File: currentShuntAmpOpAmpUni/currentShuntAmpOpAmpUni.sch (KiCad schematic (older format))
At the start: 10 parts, among them Q1 2N3906, U1 AD822A

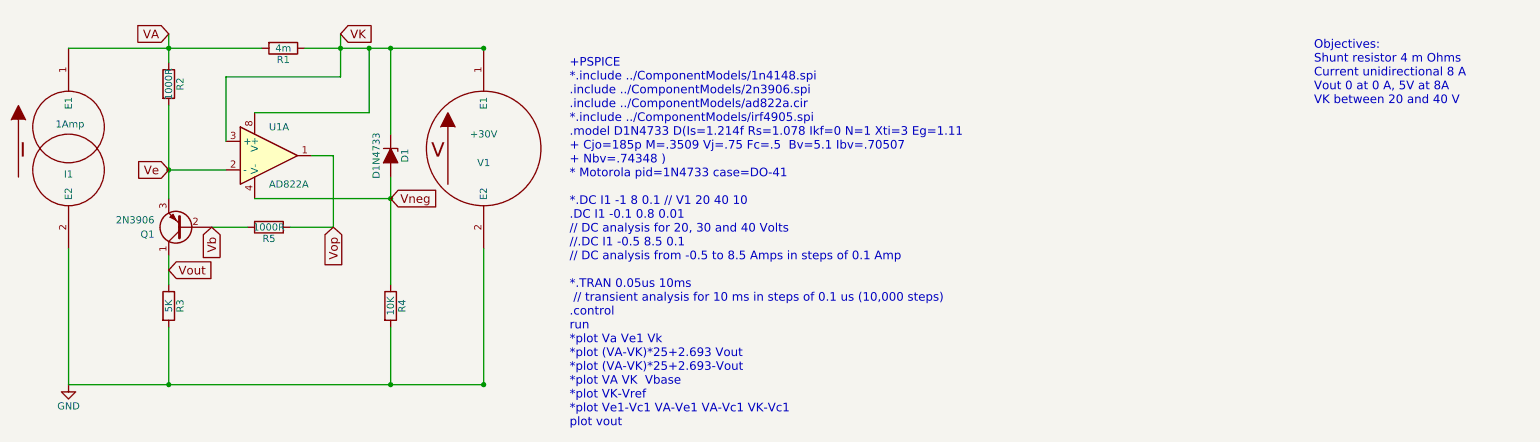
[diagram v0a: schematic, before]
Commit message: completed first current shunt amp using an op amp
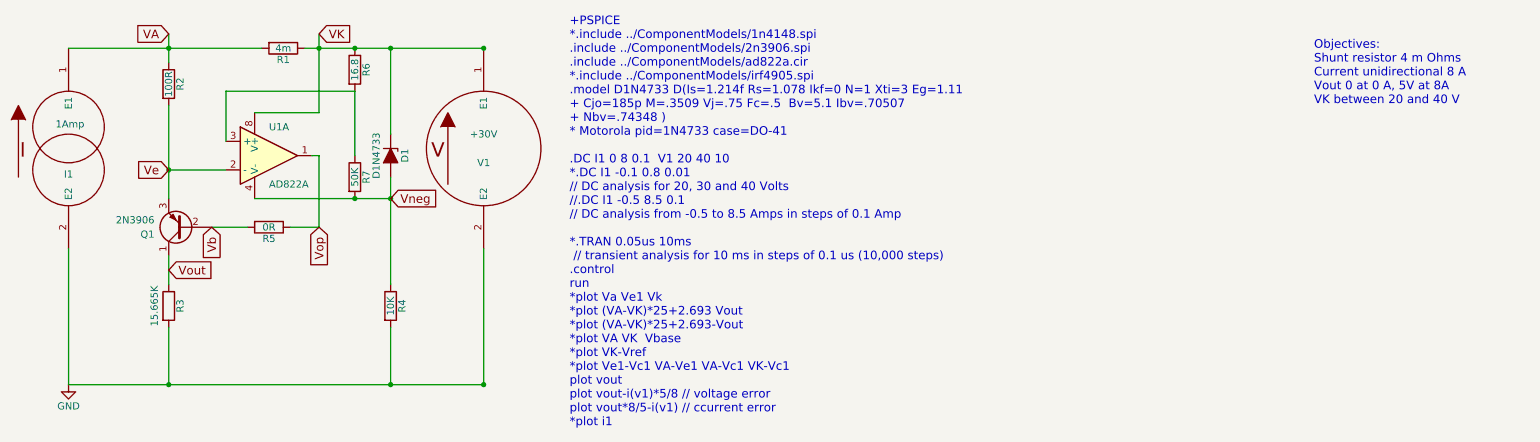
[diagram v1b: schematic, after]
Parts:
- added R6: 16.8, symbol R
- added R7: 50K, symbol R
- R2: value 1000R -> 100R
- R3: value 5K -> 15.665K
- R5: value 1000R -> 0R
- U1: Spice_Node_Sequence 8,2,3,4,1 -> 3,2,8,4,1
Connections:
- net VK: now also R6.1; no longer U1.3 (+)
- net Vneg: now also R7.2
- new net: R6.2, R7.1, U1.3 (+)
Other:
- note added: "+PSPICE \n*.include ../ComponentModels/1n4148.spi\n.include ../ComponentModels/2n3906.spi\n.include ../ComponentModels/ad822a.cir\n*.include ../ComponentModels/irf4905.spi\n.model D1N4733 D(Is=1.214f Rs=1.078 Ikf=0 N=1 Xti=3 Eg=1.11\n+ Cjo=185p M=.3509 Vj=.75 Fc=.5 Bv=5.1 Ibv=.70507\n+ Nbv=.74348 )\n* Motorola pid=1N4733 case=DO-41\n\n.DC I1 0 8 0.1 V1 20 40 10 \n*.DC I1 -0.1 0.8 0.01 \n// DC ana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"
- note removed: "+PSPICE \n*.include ../ComponentModels/1n4148.spi\n.include ../ComponentModels/2n3906.spi\n.include ../ComponentModels/ad822a.cir\n*.include ../ComponentModels/irf4905.spi\n.model D1N4733 D(Is=1.214f Rs=1.078 Ikf=0 N=1 Xti=3 Eg=1.11\n+ Cjo=185p M=.3509 Vj=.75 Fc=.5 Bv=5.1 Ibv=.70507\n+ Nbv=.74348 )\n* Motorola pid=1N4733 case=DO-41\n\n*.DC I1 -1 8 0.1 // V1 20 40 10 \n.DC I1 -0.1 0.8 0.01 \n// DC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"
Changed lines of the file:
@@
 	900  700  2250 700
 $Comp
-L GND #PWR1
+L GND #PWR01
 U 1 1 5AF292D3
 P 900 3050
-F 0 "#PWR1" H 900 2800 50  0001 C CNN
+F 0 "#PWR01" H 900 2800 50  0001 C CNN
 F 1 "GND" H 900 2900 50  0000 C CNN
 F 2 "" H 900 3050 50  0001 C CNN
@@
 $EndComp
 Text Notes 4400 3350 0    60   ~ 0
-+PSPICE \n*.include ../ComponentModels/1n4148.spi\n.include ../ComponentModels/2n3906.spi\n.include ../ComponentModels/ad822a.cir\n*.include ../ComponentModels/irf4905.spi\n.model D1N4733 D(Is=1.214f Rs=1.078 Ikf=0 N=1 Xti=3 Eg=1.11\n+ Cjo=185p M=.3509 Vj=.75 Fc=.5  Bv=5.1 Ibv=.70507\n+ Nbv=.74348 )\n* Motorola pid=1N4733 case=DO-41\n\n*.DC I1 -1 8 0.1 // V1 20 40 10 \n.DC I1 -0.1 0.8 0.01  \n// DC analysis for 20, 30 and 40 Volts\n//.DC I1 -0.5 8.5 0.1\n// DC analysis from -0.5 to 8.5 Amps in steps of 0.1 Amp\n\n*.TRAN 0.05us 10ms\n // transient analysis for 10 ms in steps of 0.1 us (10,000 steps)\n.control\nrun\n*plot Va Ve1 Vk\n*plot (VA-VK)*25+2.693 Vout\n*plot (VA-VK)*25+2.693-Vout\n*plot VA VK  Vbase\n*plot VK-Vref\n*plot Ve1-Vc1 VA-Ve1 VA-Vc1 VK-Vc1\nplot vout\n
-Connection ~ 2800 700
++PSPICE \n*.include ../ComponentModels/1n4148.spi\n.include ../ComponentModels/2n3906.spi\n.include ../ComponentModels/ad822a.cir\n*.include ../ComponentModels/irf4905.spi\n.model D1N4733 D(Is=1.214f Rs=1.078 Ikf=0 N=1 Xti=3 Eg=1.11\n+ Cjo=185p M=.3509 Vj=.75 Fc=.5  Bv=5.1 Ibv=.70507\n+ Nbv=.74348 )\n* Motorola pid=1N4733 case=DO-41\n\n.DC I1 0 8 0.1  V1 20 40 10 \n*.DC I1 -0.1 0.8 0.01  \n// DC analysis for 20, 30 and 40 Volts\n//.DC I1 -0.5 8.5 0.1\n// DC analysis from -0.5 to 8.5 Amps in steps of 0.1 Amp\n\n*.TRAN 0.05us 10ms\n // transient analysis for 10 ms in steps of 0.1 us (10,000 steps)\n.control\nrun\n*plot Va Ve1 Vk\n*plot (VA-VK)*25+2.693 Vout\n*plot (VA-VK)*25+2.693-Vout\n*plot VA VK  Vbase\n*plot VK-Vref\n*plot Ve1-Vc1 VA-Ve1 VA-Vc1 VK-Vc1\nplot vout\nplot vout-i(v1)*5/8 // voltage error\nplot vout*8/5-i(v1) // ccurrent error\n*plot i1\n
+Connection ~ 2650 700
 $Comp
 L VSOURCE V1
@@
 Text GLabel 1600 600  0    60   Input ~ 0
 VA
-Text GLabel 2800 600  2    60   Input ~ 0
+Text GLabel 2650 600  2    60   Input ~ 0
 VK
 Connection ~ 1600 700
@@
 Text Notes 9600 1100 0    60   ~ 0
 Objectives:\nShunt resistor 4 m Ohms\nCurrent unidirectional 8 A\nVout 0 at 0 A, 5V at 8A\nVK between 20 and 40 V
-Connection ~ 3000 700
 Connection ~ 3800 3050
 Connection ~ 3800 700
@@
 Wire Wire Line
 	900  3050 3800 3050
-Wire Wire Line
-	2800 600  2800 900
 $Comp
 L AD8620 U1
@@
 F 2 "" H 2300 1450 50  0001 C CNN
 F 3 "" H 2300 1450 50  0001 C CNN
-F 4 "8,2,3,4,1" H 2300 1450 60  0001 C CNN "Spice_Node_Sequence"
+F 4 "3,2,8,4,1" H 2300 1450 60  0001 C CNN "Spice_Node_Sequence"
 	1    2300 1450
 	1    0    0    -1
 $EndComp
 Wire Wire Line
-	2000 1350 2000 900
-Wire Wire Line
-	2000 900  2800 900
-Wire Wire Line
-	2200 1150 3000 1150
-Wire Wire Line
-	3000 1150 3000 700
+	2000 1350 2000 1000
+Wire Wire Line
+	2000 1000 2900 1000
+Wire Wire Line
+	2650 1150 2200 1150
+Wire Wire Line
+	2650 600  2650 1150
 $Comp
 L R R2
@@
 P 1600 950
 F 0 "R2" V 1680 950 50  0000 C CNN
-F 1 "1000R" V 1600 950 50  0000 C CNN
+F 1 "100R" V 1600 950 50  0000 C CNN
 F 2 "" V 1530 950 50  0001 C CNN
 F 3 "" H 1600 950 50  0001 C CNN
@@
 P 1600 2500
 F 0 "R3" V 1680 2500 50  0000 C CNN
-F 1 "5K" V 1600 2500 50  0000 C CNN
+F 1 "15.665K" V 1500 2500 50  0000 C CNN
 F 2 "" V 1530 2500 50  0001 C CNN
 F 3 "" H 1600 2500 50  0001 C CNN
@@
 	1600 2650 1600 3050
 Wire Wire Line
-	2750 1950 2750 1450
-Wire Wire Line
-	2750 1450 2600 1450
+	2650 1950 2650 1450
+Wire Wire Line
+	2650 1450 2600 1450
 $Comp
 L D_Zener_ALT D1
@@
 	3150 1600 3150 2350
 Wire Wire Line
-	3150 1750 2200 1750
+	2200 1750 3150 1750
 $Comp
 L R R4
@@
 P 2300 1950
 F 0 "R5" V 2380 1950 50  0000 C CNN
-F 1 "1000R" V 2300 1950 50  0000 C CNN
+F 1 "0R" V 2300 1950 50  0000 C CNN
 F 2 "" V 2230 1950 50  0001 C CNN
 F 3 "" H 2300 1950 50  0001 C CNN
@@
 $EndComp
 Wire Wire Line
-	2450 1950 2750 1950
+	2450 1950 2650 1950
 Wire Wire Line
 	2150 1950 1900 1950
-Text GLabel 2750 1950 3    60   Input ~ 0
+Text GLabel 2650 1950 3    60   Input ~ 0
 Vop
+$Comp
+L R R6
+U 1 1 5AF384A8
+P 2900 850
+F 0 "R6" V 2980 850 50  0000 C CNN
+F 1 "16.8" V 2900 850 50  0000 C CNN
+F 2 "" V 2830 850 50  0001 C CNN
+F 3 "" H 2900 850 50  0001 C CNN
+	1    2900 850
+	1    0    0    -1
+$EndComp
+$Comp
+L R R7
+U 1 1 5AF384D3
+P 2900 1600
+F 0 "R7" V 2980 1600 50  0000 C CNN
+F 1 "50K" V 2900 1600 50  0000 C CNN
+F 2 "" V 2830 1600 50  0001 C CNN
+F 3 "" H 2900 1600 50  0001 C CNN
+	1    2900 1600
+	1    0    0    -1
+$EndComp
+Connection ~ 2900 1750
+Wire Wire Line
+	2900 1000 2900 1450
+Connection ~ 2900 700
 $EndSCHEMATC

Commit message: minor updates
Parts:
- removed R5: 0R, symbol R
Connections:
- net Vop is gone; now on net Vb: U1.1
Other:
- moved on the sheet: D1, R1, R7, U1A
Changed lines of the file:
@@
 $EndDescr
 Wire Wire Line
-	900  700  2250 700
+	900  700  1850 700
 $Comp
 L GND #PWR01
@@
 Text Notes 4400 3350 0    60   ~ 0
 +PSPICE \n*.include ../ComponentModels/1n4148.spi\n.include ../ComponentModels/2n3906.spi\n.include ../ComponentModels/ad822a.cir\n*.include ../ComponentModels/irf4905.spi\n.model D1N4733 D(Is=1.214f Rs=1.078 Ikf=0 N=1 Xti=3 Eg=1.11\n+ Cjo=185p M=.3509 Vj=.75 Fc=.5  Bv=5.1 Ibv=.70507\n+ Nbv=.74348 )\n* Motorola pid=1N4733 case=DO-41\n\n.DC I1 0 8 0.1  V1 20 40 10 \n*.DC I1 -0.1 0.8 0.01  \n// DC analysis for 20, 30 and 40 Volts\n//.DC I1 -0.5 8.5 0.1\n// DC analysis from -0.5 to 8.5 Amps in steps of 0.1 Amp\n\n*.TRAN 0.05us 10ms\n // transient analysis for 10 ms in steps of 0.1 us (10,000 steps)\n.control\nrun\n*plot Va Ve1 Vk\n*plot (VA-VK)*25+2.693 Vout\n*plot (VA-VK)*25+2.693-Vout\n*plot VA VK  Vbase\n*plot VK-Vref\n*plot Ve1-Vc1 VA-Ve1 VA-Vc1 VK-Vc1\nplot vout\nplot vout-i(v1)*5/8 // voltage error\nplot vout*8/5-i(v1) // ccurrent error\n*plot i1\n
-Connection ~ 2650 700
+Connection ~ 2300 700
 $Comp
 L VSOURCE V1
@@
 Text GLabel 1600 600  0    60   Input ~ 0
 VA
-Text GLabel 2650 600  2    60   Input ~ 0
+Text GLabel 2300 600  2    60   Input ~ 0
 VK
 Connection ~ 1600 700
@@
 L R R1
 U 1 1 5AF292D9
-P 2400 700
-F 0 "R1" V 2480 700 50  0000 C CNN
-F 1 "4m" V 2400 700 50  0000 C CNN
-F 2 "" H 2400 700 50  0001 C CNN
-F 3 "" H 2400 700 50  0001 C CNN
-	1    2400 700
+P 2000 700
+F 0 "R1" V 2080 700 50  0000 C CNN
+F 1 "4m" V 2000 700 50  0000 C CNN
+F 2 "" H 2000 700 50  0001 C CNN
+F 3 "" H 2000 700 50  0001 C CNN
+	1    2000 700
 	0    1    1    0
 $EndComp
@@
 Connection ~ 1600 3050
 Wire Wire Line
-	2550 700  3800 700
+	2150 700  3800 700
 Wire Wire Line
 	900  3050 3800 3050
@@
 L AD8620 U1
 U 1 1 5AF2A4C1
-P 2300 1450
-F 0 "U1" H 2300 1650 50  0000 L CNN
-F 1 "AD822A" H 2300 1250 50  0000 L CNN
-F 2 "" H 2300 1450 50  0001 C CNN
-F 3 "" H 2300 1450 50  0001 C CNN
-F 4 "3,2,8,4,1" H 2300 1450 60  0001 C CNN "Spice_Node_Sequence"
-	1    2300 1450
-	1    0    0    -1
-$EndComp
-Wire Wire Line
-	2000 1350 2000 1000
-Wire Wire Line
-	2000 1000 2900 1000
-Wire Wire Line
-	2650 1150 2200 1150
-Wire Wire Line
-	2650 600  2650 1150
+P 2200 1200
+F 0 "U1" H 2200 1400 50  0000 L CNN
+F 1 "AD822A" H 2200 1000 50  0000 L CNN
+F 2 "" H 2200 1200 50  0001 C CNN
+F 3 "" H 2200 1200 50  0001 C CNN
+F 4 "3,2,8,4,1" H 2200 1200 60  0001 C CNN "Spice_Node_Sequence"
+	1    2200 1200
+	-1   0    0    -1
+$EndComp
+Wire Wire Line
+	2500 1100 2900 1100
+Wire Wire Line
+	2300 600  2300 900
 $Comp
 L R R2
@@
 	1600 1100 1600 1750
 Wire Wire Line
-	1600 1550 2000 1550
+	1600 1650 2500 1650
 $Comp
 L Q_PNP_CBE Q1
@@
 	-1   0    0    1
 $EndComp
-Connection ~ 1600 1550
+Connection ~ 1600 1650
 $Comp
 L R R3
@@
 Wire Wire Line
 	1600 2650 1600 3050
-Wire Wire Line
-	2650 1950 2650 1450
-Wire Wire Line
-	2650 1450 2600 1450
 $Comp
 L D_Zener_ALT D1
 U 1 1 5AF2AC64
-P 3150 1450
-F 0 "D1" H 3150 1550 50  0000 C CNN
-F 1 "D1N4733" H 3150 1350 50  0000 C CNN
-F 2 "" H 3150 1450 50  0001 C CNN
-F 3 "" H 3150 1450 50  0001 C CNN
-F 4 "2,1" H 3150 1450 60  0001 C CNN "Spice_Node_Sequence"
-	1    3150 1450
+P 3150 1250
+F 0 "D1" H 3150 1350 50  0000 C CNN
+F 1 "D1N4733" H 3150 1150 50  0000 C CNN
+F 2 "" H 3150 1250 50  0001 C CNN
+F 3 "" H 3150 1250 50  0001 C CNN
+F 4 "2,1" H 3150 1250 60  0001 C CNN "Spice_Node_Sequence"
+	1    3150 1250
 	0    1    1    0
 $EndComp
 Wire Wire Line
-	3150 1300 3150 700
+	3150 1100 3150 700
 Connection ~ 3150 700
 Wire Wire Line
-	3150 1600 3150 2350
-Wire Wire Line
-	2200 1750 3150 1750
+	3150 1400 3150 2350
+Wire Wire Line
+	2300 1500 3150 1500
 $Comp
 L R R4
@@
 	1    0    0    -1
 $EndComp
-Connection ~ 3150 1750
+Connection ~ 3150 1500
 Wire Wire Line
 	3150 2650 3150 3050
@@
 Text GLabel 1600 2250 2    60   Input ~ 0
 Vout
-Text GLabel 1900 1950 3    60   Input ~ 0
+Text GLabel 1900 1950 2    60   Input ~ 0
 Vb
-Text GLabel 1600 1550 0    60   Input ~ 0
+Text GLabel 1600 1650 0    60   Input ~ 0
 Ve
-Text GLabel 3150 1750 2    60   Input ~ 0
+Text GLabel 3150 1500 2    60   Input ~ 0
 Vneg
-$Comp
-L R R5
-U 1 1 5AF2E738
-P 2300 1950
-F 0 "R5" V 2380 1950 50  0000 C CNN
-F 1 "0R" V 2300 1950 50  0000 C CNN
-F 2 "" V 2230 1950 50  0001 C CNN
-F 3 "" H 2300 1950 50  0001 C CNN
-	1    2300 1950
-	0    1    1    0
-$EndComp
-Wire Wire Line
-	2450 1950 2650 1950
-Wire Wire Line
-	2150 1950 1900 1950
-Text GLabel 2650 1950 3    60   Input ~ 0
-Vop
+Wire Wire Line
+	1900 1950 1900 1950
 $Comp
 L R R6
@@
 L R R7
 U 1 1 5AF384D3
-P 2900 1600
-F 0 "R7" V 2980 1600 50  0000 C CNN
-F 1 "50K" V 2900 1600 50  0000 C CNN
-F 2 "" V 2830 1600 50  0001 C CNN
-F 3 "" H 2900 1600 50  0001 C CNN
-	1    2900 1600
-	1    0    0    -1
-$EndComp
-Connection ~ 2900 1750
-Wire Wire Line
-	2900 1000 2900 1450
+P 2900 1350
+F 0 "R7" V 2980 1350 50  0000 C CNN
+F 1 "50K" V 2900 1350 50  0000 C CNN
+F 2 "" V 2830 1350 50  0001 C CNN
+F 3 "" H 2900 1350 50  0001 C CNN
+	1    2900 1350
+	1    0    0    -1
+$EndComp
+Connection ~ 2900 1500
+Wire Wire Line
+	2900 1000 2900 1200
 Connection ~ 2900 700
+Connection ~ 2900 1100
+Wire Wire Line
+	1900 1200 1900 1950
+Wire Wire Line
+	2500 1650 2500 1300
 $EndSCHEMATC
